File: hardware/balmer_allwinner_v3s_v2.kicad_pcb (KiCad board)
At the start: 4 copper layers, 60 x 60 mm, 119 parts, among them J1 JAE_SIM_Card_SF72S006, J11 Micro_SD_Card_Ebay, J2 UART, J3 Bus_PCI_Express_Mini, J4 USB_C_Receptacle, J8 HR911105_RJ45, SW2 SW_MEC_5G, U1 AllwinnerV3S, U10 TLV62568DBV, U2 CH340C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

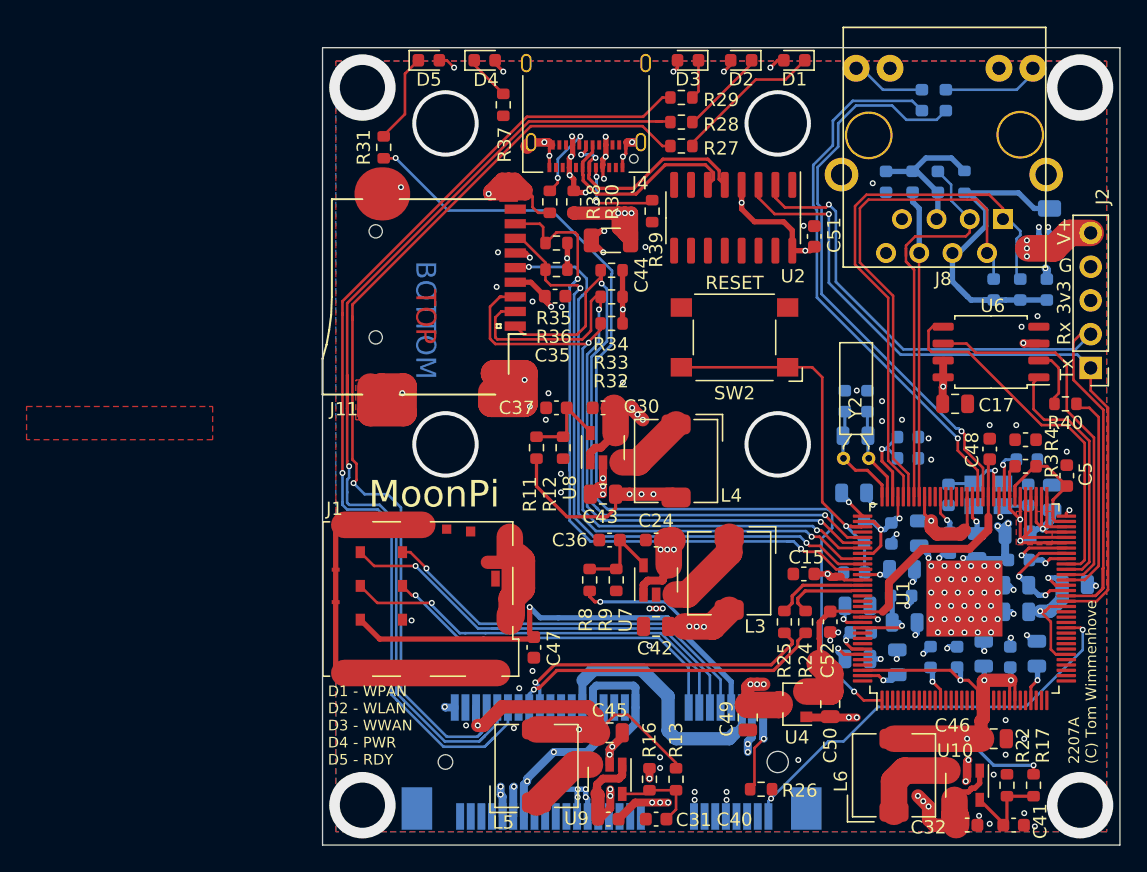
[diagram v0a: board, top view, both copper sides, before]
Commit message: Removed mask and added vias around mounting pads
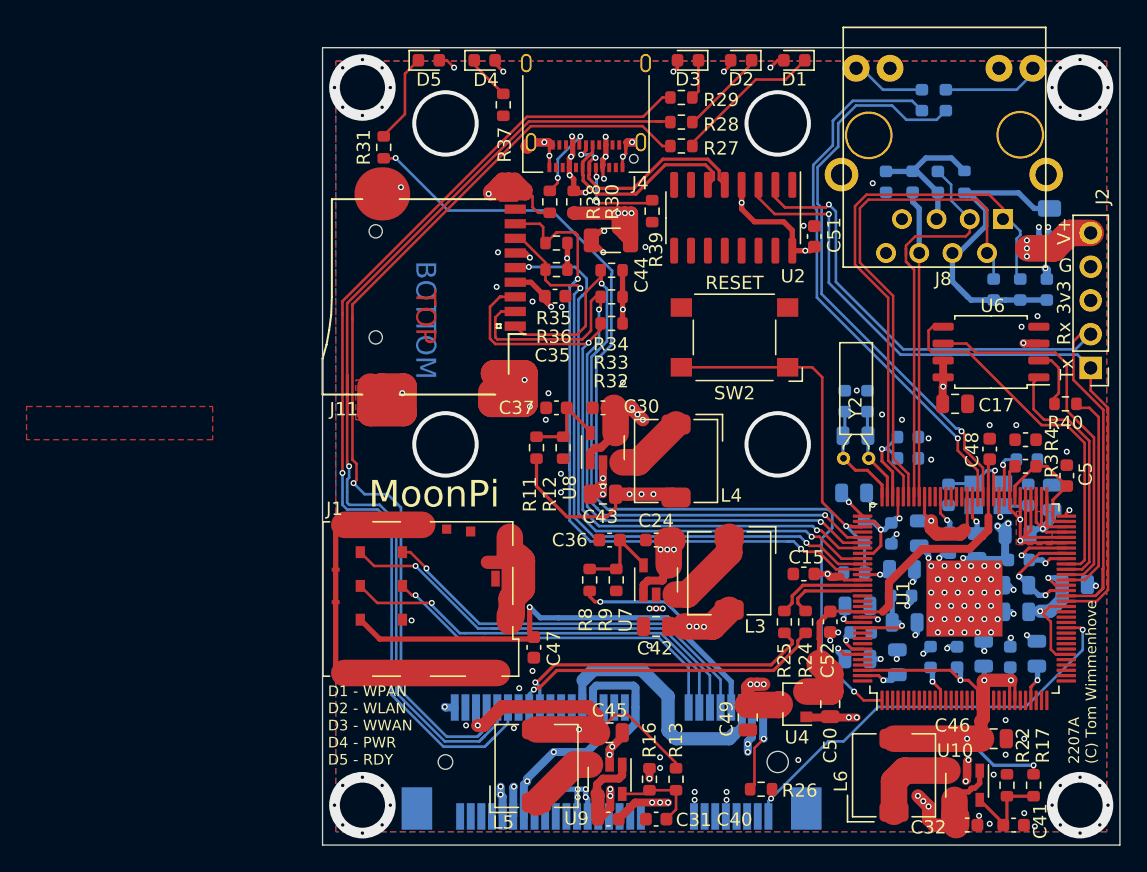
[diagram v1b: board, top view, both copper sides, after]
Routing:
- net GND: vias 141 -> 173
- net (no net): vias 1 -> 0
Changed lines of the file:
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@@
   (general
     (thickness 1.6)
-    (drawings 19)
-    (tracks 1587)
+    (drawings 27)
+    (tracks 1618)
     (zones 0)
     (modules 119)
@@
     (tags resistor)
     (attr smd)
-    (fp_text reference R10 (at -2.5 0.072 90) (layer B.SilkS)
+    (fp_text reference R10 (at 2.1 0 270) (layer B.SilkS)
       (effects (font (size 1 1) (thickness 0.15)) (justify mirror))
     )
@@
     )
   )
+  (gr_circle (center 65 78) (end 67.1 78) (layer B.Mask) (width 0.8))
+  (gr_circle (center 119 78) (end 121.1 78) (layer B.Mask) (width 0.8))
+  (gr_circle (center 119 132) (end 121.1 132) (layer B.Mask) (width 0.8))
+  (gr_circle (center 65 132) (end 67.1 132) (layer B.Mask) (width 0.8))
+  (gr_circle (center 65 132) (end 67.1 132) (layer F.Mask) (width 0.8))
+  (gr_circle (center 119 132) (end 121.1 132) (layer F.Mask) (width 0.8))
+  (gr_circle (center 119 78) (end 121.1 78) (layer F.Mask) (width 0.8))
+  (gr_circle (center 65 78) (end 67.1 78) (layer F.Mask) (width 0.8))
   (gr_circle (center 71.25 104.85) (end 74.2 104.85) (layer B.Mask) (width 1.5))
   (gr_circle (center 96.25 104.85) (end 99.2 104.85) (layer B.Mask) (width 1.5))
@@
   (gr_line (start 62 75) (end 122 75) (layer Edge.Cuts) (width 0.05))
   (gr_line (start 62 135) (end 62 75) (layer Edge.Cuts) (width 0.05))
-  (via (at 104.1 101.6) (size 0.45) (drill 0.25) (layers F.Cu B.Cu) (net 0))
+  (via (at 116.9 78) (size 0.45) (drill 0.25) (layers F.Cu B.Cu) (net 1))
+  (via (at 119 80.1) (size 0.45) (drill 0.25) (layers F.Cu B.Cu) (net 1))
+  (via (at 121.1 78) (size 0.45) (drill 0.25) (layers F.Cu B.Cu) (net 1))
+  (via (at 119 75.9) (size 0.45) (drill 0.25) (layers F.Cu B.Cu) (net 1))
+  (via (at 117.515076 76.515076) (size 0.45) (drill 0.25) (layers F.Cu B.Cu) (net 1))
+  (via (at 117.515076 79.484924) (size 0.45) (drill 0.25) (layers F.Cu B.Cu) (net 1))
+  (via (at 120.484924 79.484924) (size 0.45) (drill 0.25) (layers F.Cu B.Cu) (net 1))
+  (via (at 120.484924 76.515076) (size 0.45) (drill 0.25) (layers F.Cu B.Cu) (net 1))
+  (via (at 62.9 78) (size 0.45) (drill 0.25) (layers F.Cu B.Cu) (net 1))
+  (via (at 66.484924 79.484924) (size 0.45) (drill 0.25) (layers F.Cu B.Cu) (net 1))
+  (via (at 66.484924 76.515076) (size 0.45) (drill 0.25) (layers F.Cu B.Cu) (net 1))
+  (via (at 65 75.9) (size 0.45) (drill 0.25) (layers F.Cu B.Cu) (net 1))
+  (via (at 63.515076 79.484924) (size 0.45) (drill 0.25) (layers F.Cu B.Cu) (net 1))
+  (via (at 67.1 78) (size 0.45) (drill 0.25) (layers F.Cu B.Cu) (net 1))
+  (via (at 63.515076 76.515076) (size 0.45) (drill 0.25) (layers F.Cu B.Cu) (net 1))
+  (via (at 65 80.1) (size 0.45) (drill 0.25) (layers F.Cu B.Cu) (net 1))
+  (via (at 62.9 132) (size 0.45) (drill 0.25) (layers F.Cu B.Cu) (net 1))
+  (via (at 66.484924 133.484924) (size 0.45) (drill 0.25) (layers F.Cu B.Cu) (net 1))
+  (via (at 66.484924 130.515076) (size 0.45) (drill 0.25) (layers F.Cu B.Cu) (net 1))
+  (via (at 65 129.9) (size 0.45) (drill 0.25) (layers F.Cu B.Cu) (net 1))
+  (via (at 63.515076 133.484924) (size 0.45) (drill 0.25) (layers F.Cu B.Cu) (net 1))
+  (via (at 67.1 132) (size 0.45) (drill 0.25) (layers F.Cu B.Cu) (net 1))
+  (via (at 63.515076 130.515076) (size 0.45) (drill 0.25) (layers F.Cu B.Cu) (net 1))
+  (via (at 65 134.1) (size 0.45) (drill 0.25) (layers F.Cu B.Cu) (net 1))
+  (via (at 116.9 132) (size 0.45) (drill 0.25) (layers F.Cu B.Cu) (net 1))
+  (via (at 120.484924 133.484924) (size 0.45) (drill 0.25) (layers F.Cu B.Cu) (net 1))
+  (via (at 120.484924 130.515076) (size 0.45) (drill 0.25) (layers F.Cu B.Cu) (net 1))
+  (via (at 119 129.9) (size 0.45) (drill 0.25) (layers F.Cu B.Cu) (net 1))
+  (via (at 117.515076 133.484924) (size 0.45) (drill 0.25) (layers F.Cu B.Cu) (net 1))
+  (via (at 121.1 132) (size 0.45) (drill 0.25) (layers F.Cu B.Cu) (net 1))
+  (via (at 117.515076 130.515076) (size 0.45) (drill 0.25) (layers F.Cu B.Cu) (net 1))
+  (via (at 119 134.1) (size 0.45) (drill 0.25) (layers F.Cu B.Cu) (net 1))
   (via (at 65 132) (size 5) (drill 3.4) (layers F.Cu B.Cu) (net 1))
   (via (at 119 78) (size 5) (drill 3.4) (layers F.Cu B.Cu) (net 1))
@@
   (via (at 107.6 104.4) (size 0.45) (drill 0.25) (layers F.Cu B.Cu) (net 1))
   (via (at 102.2 100.8) (size 0.45) (drill 0.25) (layers F.Cu B.Cu) (net 1))
-  (via (at 104.1 103.1) (size 0.45) (drill 0.25) (layers F.Cu B.Cu) (net 1))
+  (via (at 104.1 102.6) (size 0.45) (drill 0.25) (layers F.Cu B.Cu) (net 1))
   (via (at 103.4 85.2) (size 0.45) (drill 0.25) (layers F.Cu B.Cu) (net 1))
   (via (at 78.8 103) (size 0.45) (drill 0.25) (layers F.Cu B.Cu) (net 1))

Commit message: Better mechanical support on GND pads for mPCIe conn
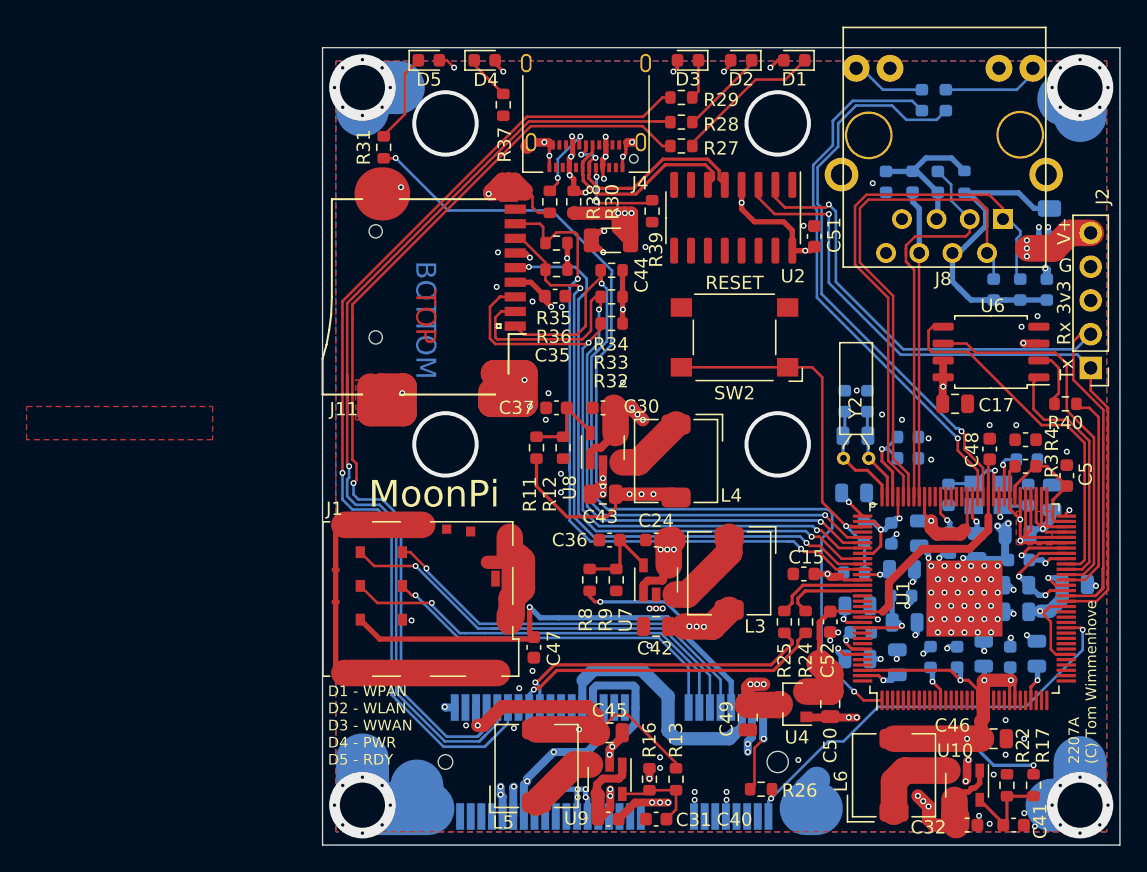
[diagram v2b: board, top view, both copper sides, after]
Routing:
- net GND: track 160.9 -> 189.9 mm

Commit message: Minor touch-ups
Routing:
- net +3V3: track 170.6 -> 174.4 mm
- net SDC0_D2: track 50.5 -> 47.0 mm
- net SDC0_D3: track 51.9 -> 48.9 mm
- net SDC1_D2: track 73.7 -> 75.7 mm
- net /SVREF: track 10.1 -> 12.1 mm
- net GND: track 189.9 -> 191.7 mm, vias 173 -> 174
- net +1V5: track 47.5 -> 48.2 mm, vias 2 -> 3
- net VCC: vias 23 -> 22

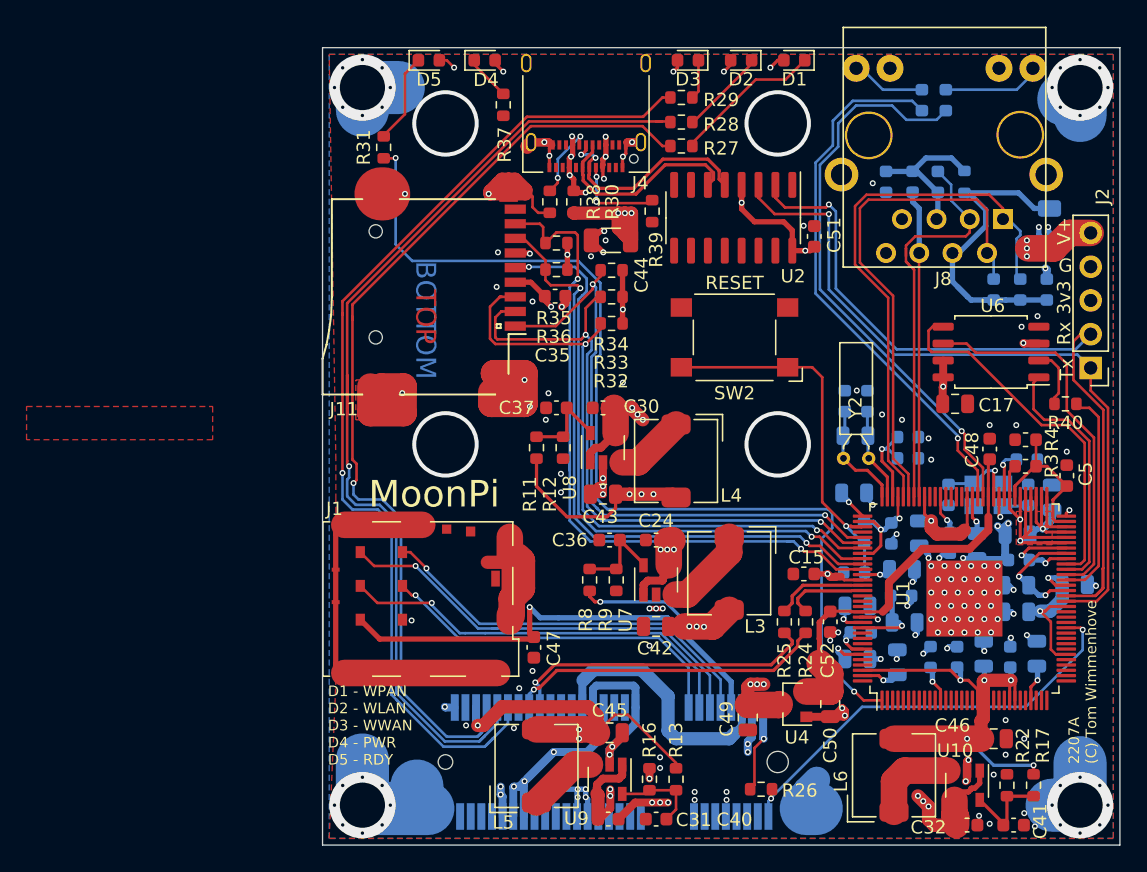
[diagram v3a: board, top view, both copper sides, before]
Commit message: Added 0R for USB_ID pin + Moved OK LED to licheePi default GPIO
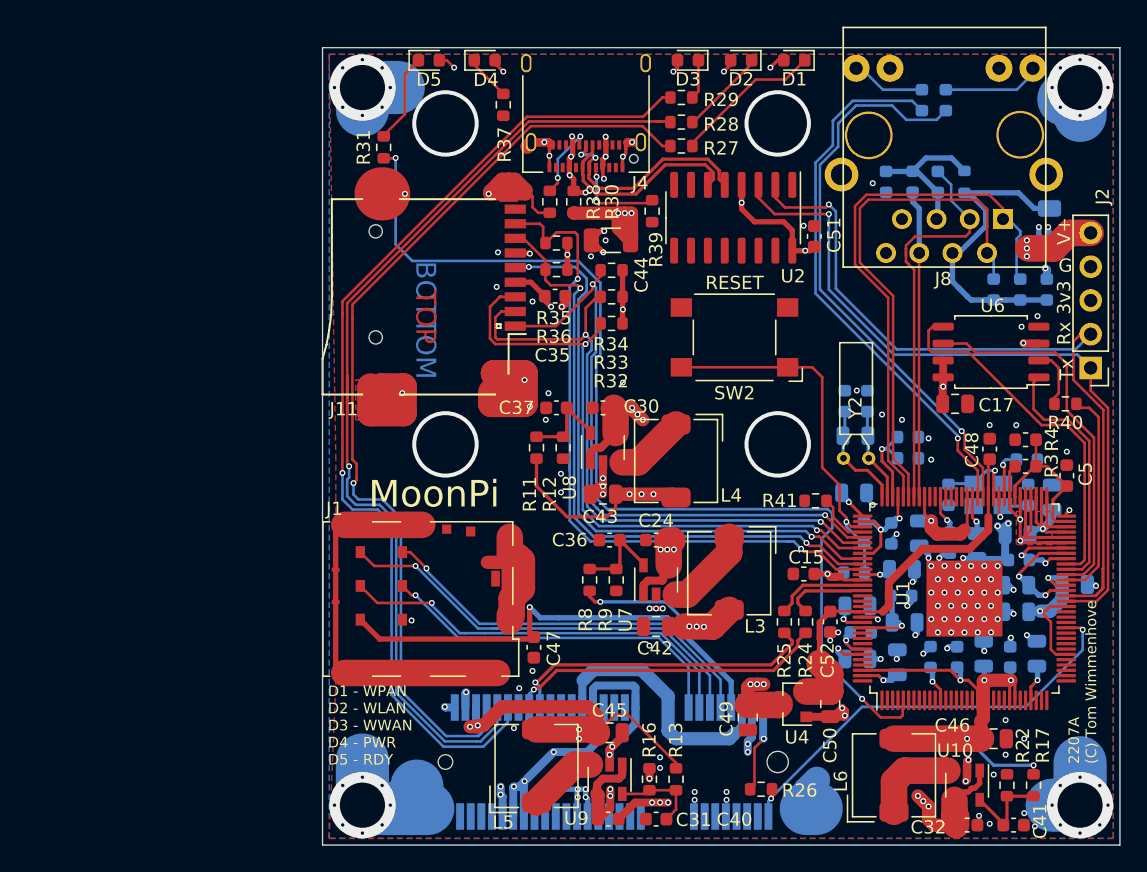
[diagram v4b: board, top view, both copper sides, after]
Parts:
- added R41: 0R, Resistor_SMD:R_0603_1608Metric, F.Cu at (99.1, 109.1)
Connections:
- R31 pad 2: SDC1_D2 -> SDC1_CLK
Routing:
- net SDC1_CLK: track 0.00 -> 79.1 mm, vias 0 -> 2
- net SDC1_D2: track 75.7 -> 0.00 mm, vias 2 -> 0
- net USB-ID: track 0.00 -> 4.11 mm
- net GND: track 191.7 -> 192.9 mm
- net +1V5: track 48.2 -> 49.4 mm, vias 3 -> 4
- net Net-(J3-Pad42): track 76.4 -> 75.6 mm

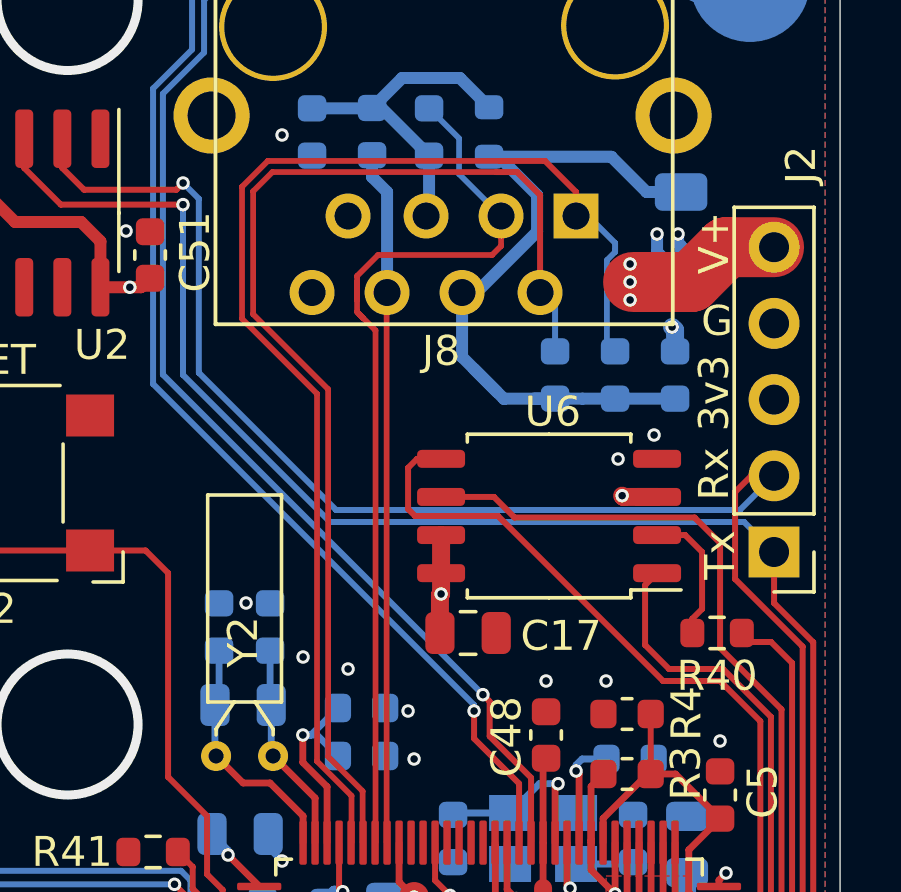
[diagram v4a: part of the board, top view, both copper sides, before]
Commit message: Added T-PAD below NAND Flash
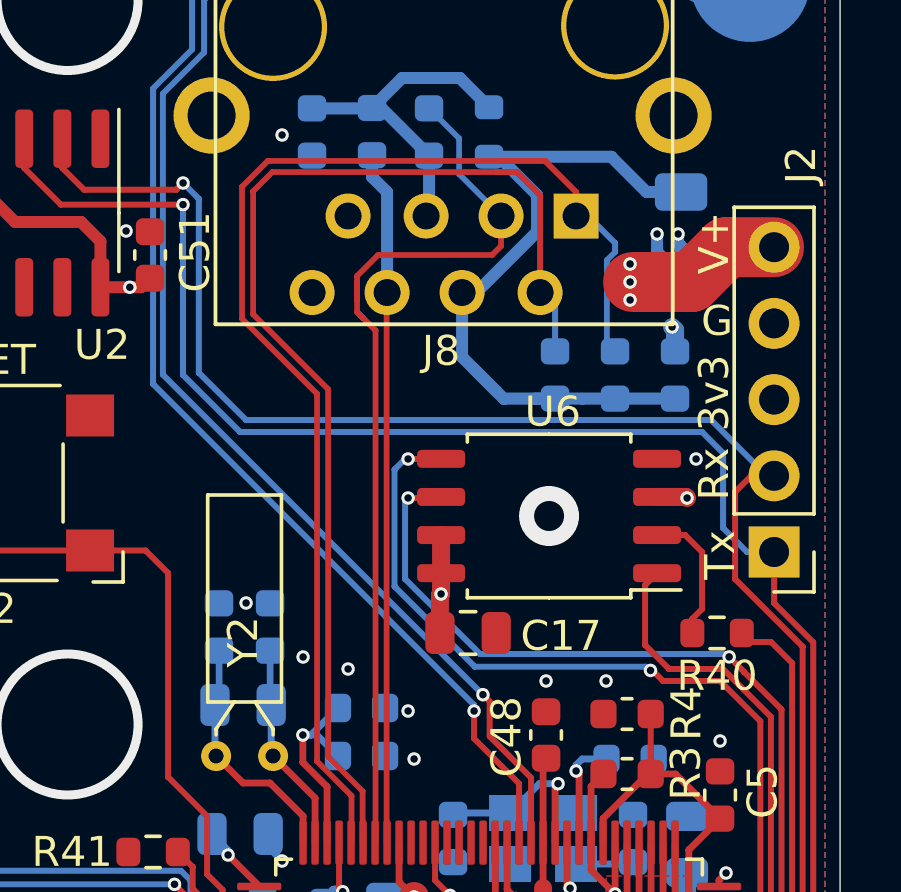
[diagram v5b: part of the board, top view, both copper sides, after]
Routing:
- net SPI_MOSI: track 27.6 -> 30.0 mm, vias 0 -> 2
- net SPI_SCK: track 28.3 -> 30.1 mm, vias 0 -> 2
- net UART0_TX: track 55.3 -> 56.8 mm
- net UART0_RX: track 59.9 -> 58.9 mm
